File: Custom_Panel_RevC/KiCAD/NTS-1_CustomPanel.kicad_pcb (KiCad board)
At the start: 2 copper layers, 128.5 x 78 mm, 67 parts, among them CN1 19x2 2.54mm header, CN10 1x4 2.54mm header, CN11 1x3 2.54mm header, CN2 1x7 2.54mm header, CN3 1x8 2.54mm connector, CN4 1x6 2.54mm connector, CN5 1x10 2.54mm connector, CN6 1x8 2.54mm connector, CN7 1x7 2.54mm header, CN8 19x2 2.54mm header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

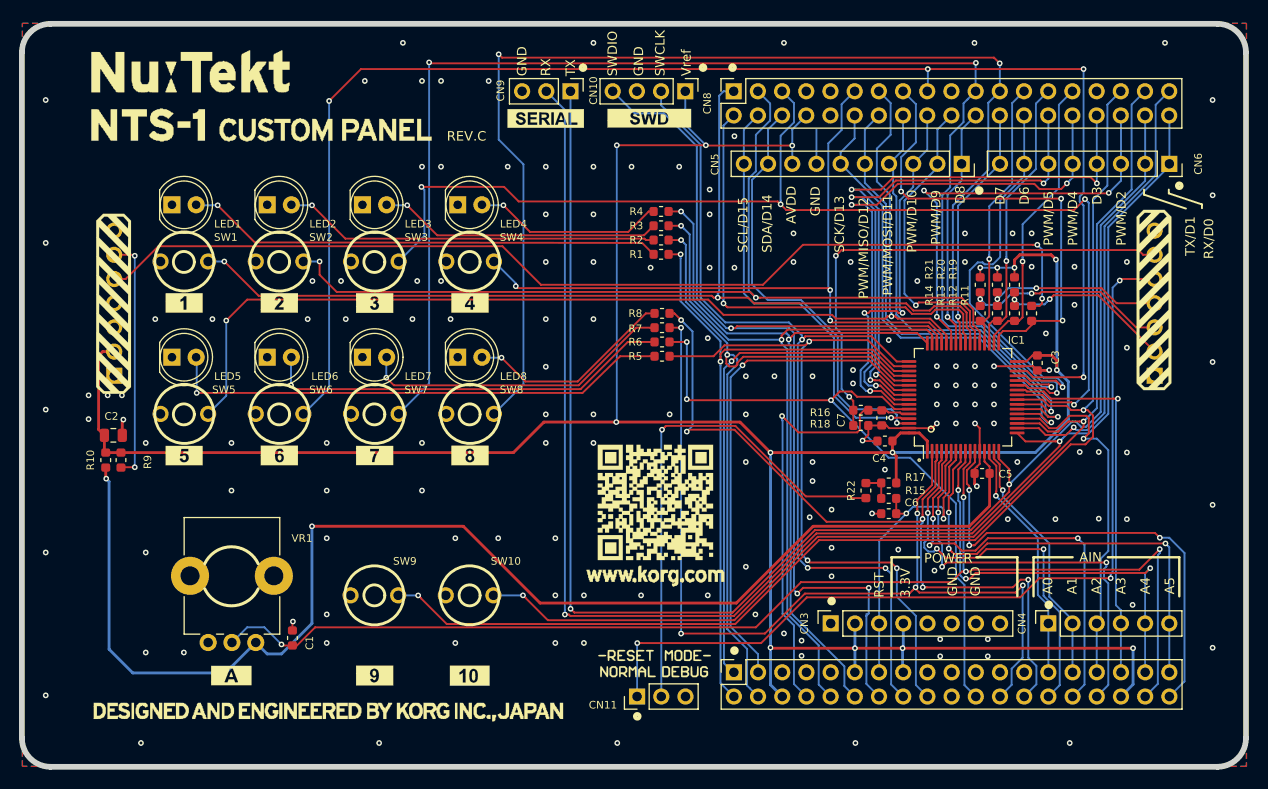
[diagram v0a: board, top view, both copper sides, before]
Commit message: Updated to more common components.
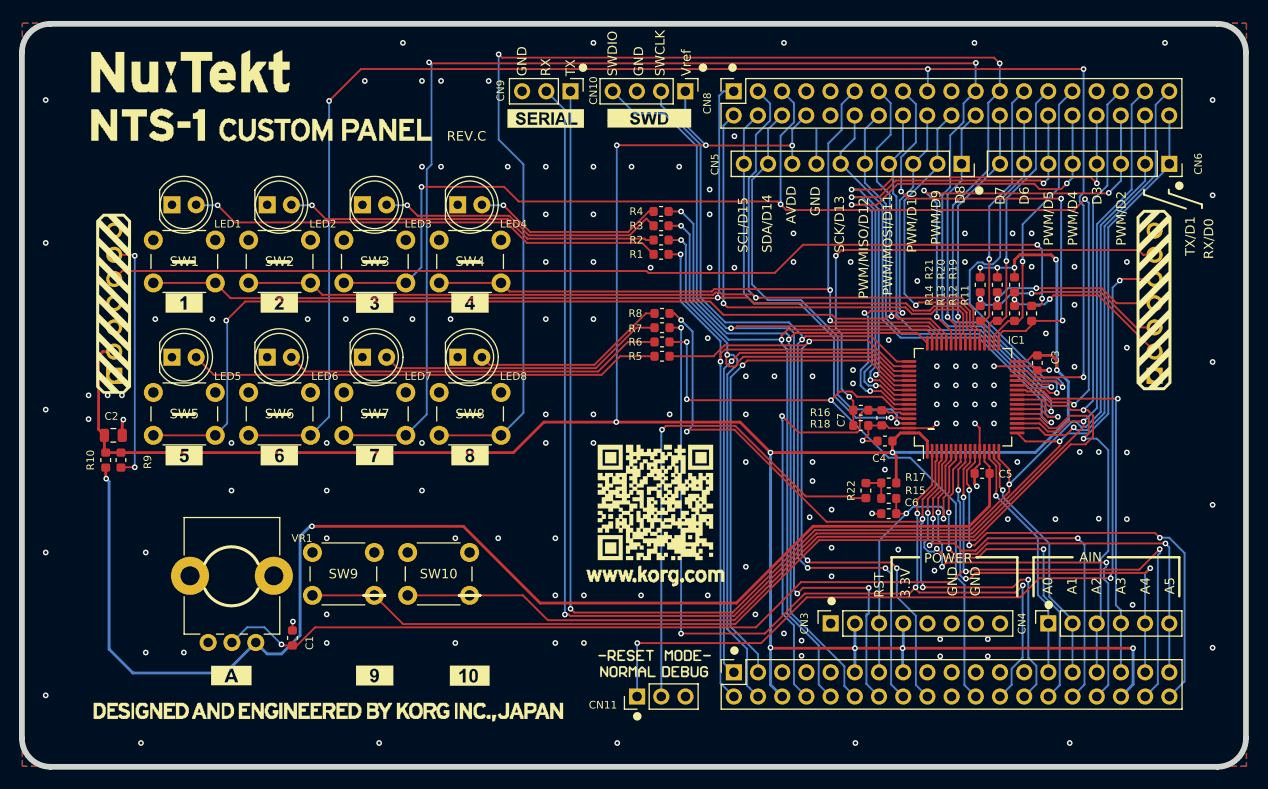
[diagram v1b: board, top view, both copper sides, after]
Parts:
- SW1, SW10, SW2, SW3, SW4, SW5, SW6, SW7, SW8, SW9: footprint CustomPanel:SW_Tactile_SKRH -> Button_Switch_THT:SW_PUSH_6mm
- moved SW2 3.95 mm to (130.3, 99.2)
- moved SW6 3.95 mm to (130.3, 115.2)
- moved SW1 3.95 mm to (120.3, 99.2)
- moved SW3 3.95 mm to (140.3, 99.2)
- moved SW4 3.95 mm to (150.3, 99.2)
- moved SW5 3.95 mm to (120.3, 115.2)
- moved SW7 3.95 mm to (140.3, 115.2)
- moved SW8 3.95 mm to (150.3, 115.2)
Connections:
- net /~RESET_PNL renamed /~{RESET_PNL}
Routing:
- net /PF5: track 117.1 -> 126.1 mm, vias 2 -> 1
- net /PC4: track 128.3 -> 137.3 mm, vias 2 -> 1
- net /PB2: track 142.4 -> 151.0 mm
- net /PB1: track 141.2 -> 149.7 mm
- net /PB11: track 156.8 -> 165.3 mm
- net /PA11: track 115.1 -> 123.4 mm
- net /PC5: track 122.0 -> 130.2 mm
- net /PC8: track 108.6 -> 113.4 mm, vias 2 -> 1
- net /PA12: track 75.2 -> 80.1 mm, vias 3 -> 2
- net /PC6: track 100.5 -> 104.7 mm, vias 2 -> 1
- net Net-(LED5-Pad2): track 53.4 -> 49.8 mm, vias 1 -> 0
- net Net-(LED6-Pad2): track 43.3 -> 40.1 mm, vias 1 -> 0
- net /PANEL_ACK: track 109.3 -> 106.1 mm
- net Net-(LED7-Pad2): track 33.6 -> 30.9 mm, vias 1 -> 0
- net Net-(LED8-Pad2): track 22.1 -> 20.8 mm, vias 1 -> 0
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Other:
- net class Default removed
- board text added: "JLCJLCJLCJLC"
